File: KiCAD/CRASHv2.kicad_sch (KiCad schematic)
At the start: 2 parts, among them U1 ATmega32A-A, U2 LM317_SOT-223

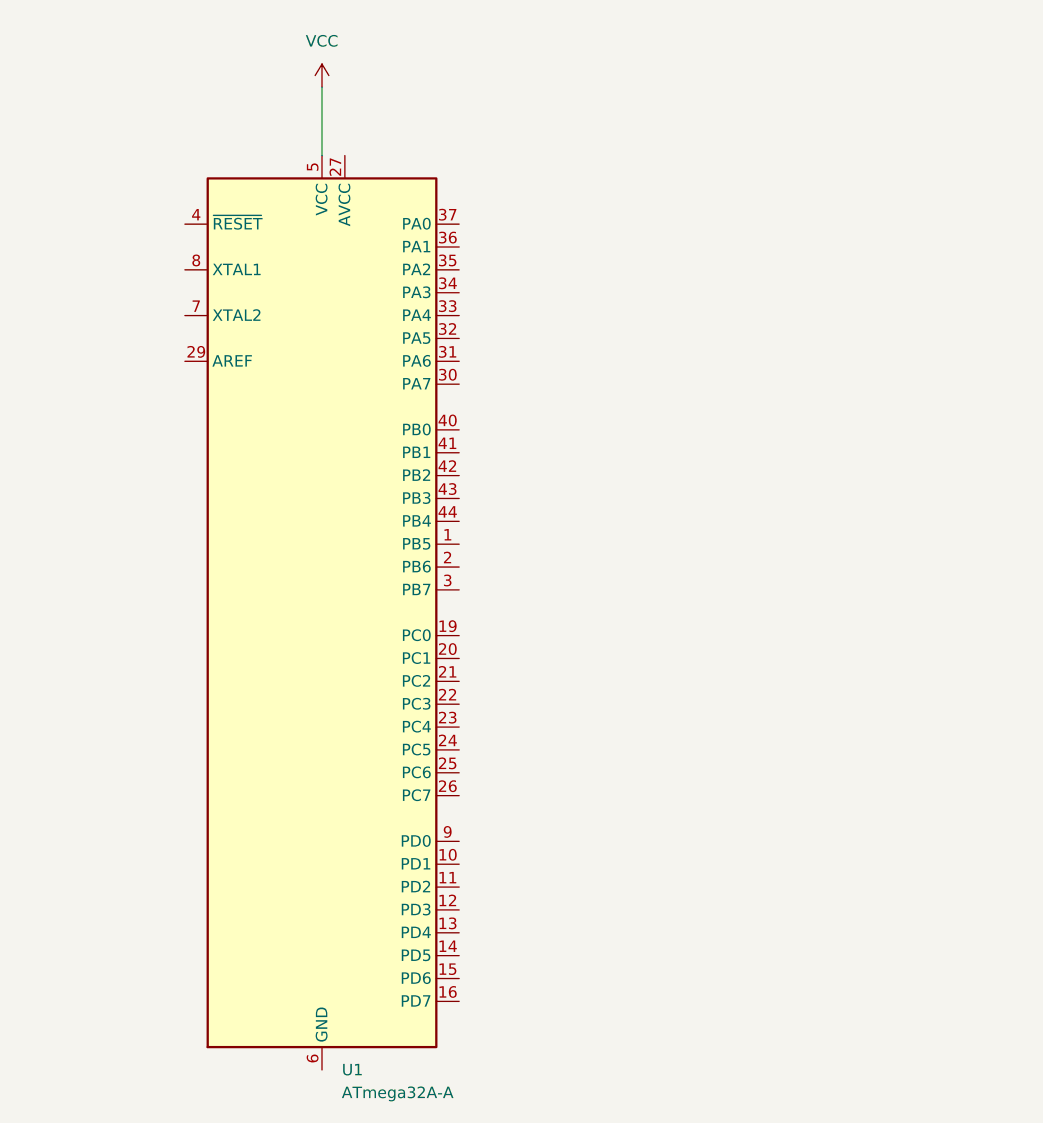
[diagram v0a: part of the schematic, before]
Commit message: Atmega ports for USB, nrf24 & gimble inputs
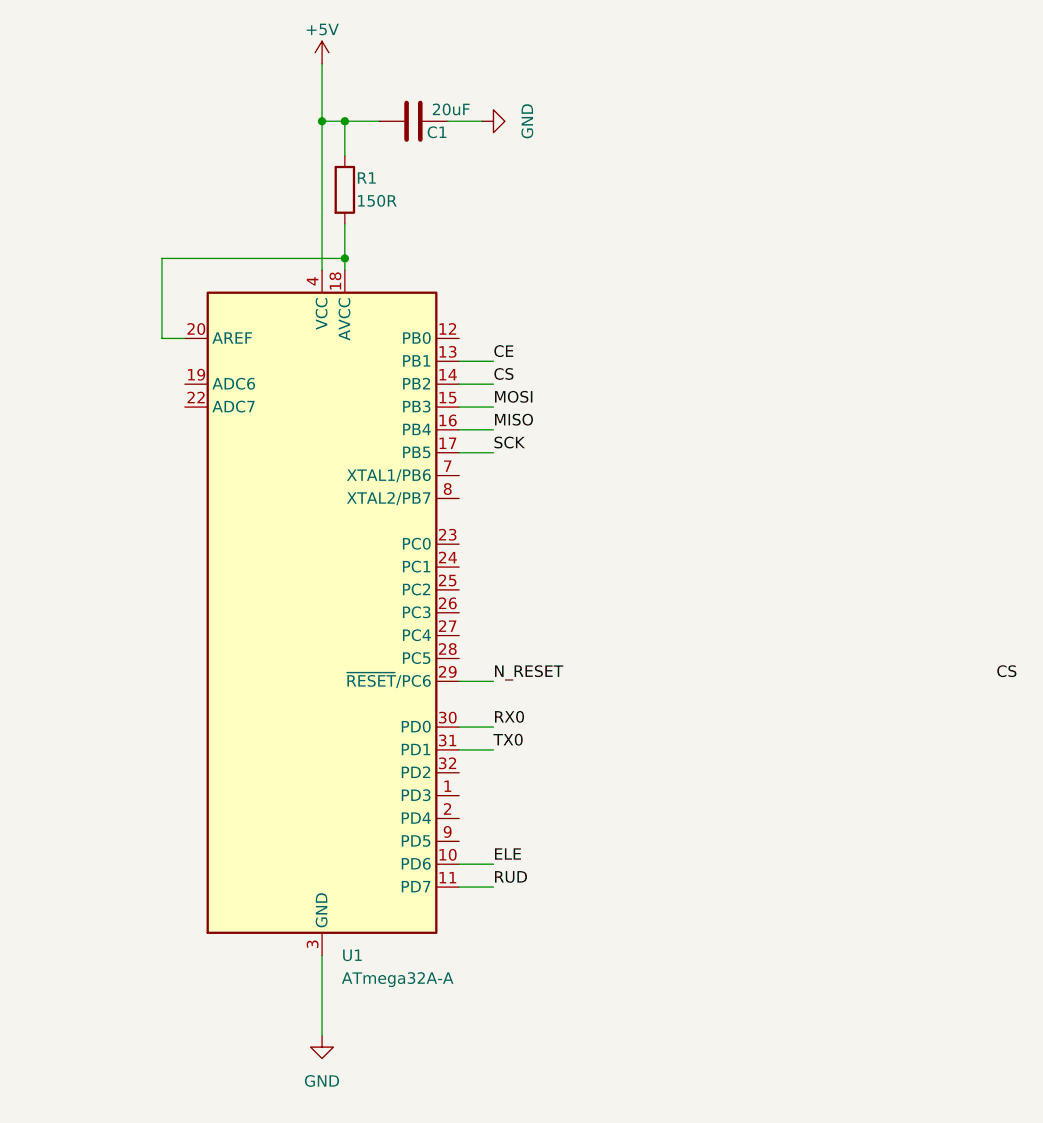
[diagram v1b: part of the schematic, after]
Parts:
- added C1: 20uF, symbol Device:C
- added R1: 150R, symbol Device:R
- U1: footprint Package_QFP:TQFP-44_10x10mm_P0.8mm -> Package_QFP:TQFP-32_7x7mm_P0.8mm; symbol MCU_Microchip_ATmega:ATmega32A-A -> MCU_Microchip_ATmega:ATmega328P-A
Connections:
- net ELE: now reaches U1.10 (PD6)
- net RUD: now reaches U1.11 (PD7)
- net CE: now reaches U1.13 (PB1)
- net CS: now reaches U1.14 (PB2)
- net MOSI: now reaches U1.15 (PB3)
- net MISO: now reaches U1.16 (PB4)
- net at U1.20 (AREF): now also U1.18 (AVCC), R1.2
- net GND: now reaches U1.21 (GND)
- net GND: now also U1.3 (GND), U1.5 (GND), C1.2
- net N_RESET: now reaches U1.29 (~{RESET}/PC6)
- net RX0: now reaches U1.30 (PD0)
- net TX0: now reaches U1.31 (PD1)
- net +5V: now reaches U1.4 (VCC)
- net +5V: now also U1.6 (VCC), C1.1, R1.1
- removed net VCC: U1.17 (VCC), U1.38 (VCC), U1.5 (VCC)
- new net SCK: U1.17 (PB5)
- now unconnected: U1.28 (GND)
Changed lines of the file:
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@@
 (kicad_sch (version 20230121) (generator eeschema)
   (paper "A4")
-  (wire (pts (xy 243.84 20.32) (xy 243.84 27.94))
-    (stroke (width 0) (type default))
+  (junction (at 246.38 24.13) (diameter 0) (color 0 0 0 0)
+  )
+  (junction (at 246.38 39.37) (diameter 0) (color 0 0 0 0)
+  )
+  (junction (at 243.84 24.13) (diameter 0) (color 0 0 0 0)
+  )
+  (wire (pts (xy 259.08 106.68) (xy 262.89 106.68))
+    (stroke (width 0) (type default))
+  )
+  (wire (pts (xy 259.08 53.34) (xy 262.89 53.34))
+    (stroke (width 0) (type default))
+  )
+  (wire (pts (xy 243.84 116.84) (xy 243.84 125.73))
+    (stroke (width 0) (type default))
+  )
+  (wire (pts (xy 259.08 86.36) (xy 262.89 86.36))
+    (stroke (width 0) (type default))
+  )
+  (wire (pts (xy 246.38 39.37) (xy 246.38 40.64))
+    (stroke (width 0) (type default))
+  )
+  (wire (pts (xy 246.38 24.13) (xy 250.19 24.13))
+    (stroke (width 0) (type default))
+  )
+  (wire (pts (xy 259.08 109.22) (xy 262.89 109.22))
+    (stroke (width 0) (type default))
+  )
+  (wire (pts (xy 228.6 48.26) (xy 226.06 48.26))
+    (stroke (width 0) (type default))
+  )
+  (wire (pts (xy 243.84 24.13) (xy 246.38 24.13))
+    (stroke (width 0) (type default))
+  )
+  (wire (pts (xy 243.84 24.13) (xy 243.84 40.64))
+    (stroke (width 0) (type default))
+  )
+  (wire (pts (xy 246.38 35.56) (xy 246.38 39.37))
+    (stroke (width 0) (type default))
+  )
+  (wire (pts (xy 259.08 50.8) (xy 262.89 50.8))
+    (stroke (width 0) (type default))
+  )
+  (wire (pts (xy 259.08 58.42) (xy 262.89 58.42))
+    (stroke (width 0) (type default))
+  )
+  (wire (pts (xy 259.08 55.88) (xy 262.89 55.88))
+    (stroke (width 0) (type default))
+  )
+  (wire (pts (xy 246.38 24.13) (xy 246.38 27.94))
+    (stroke (width 0) (type default))
+  )
+  (wire (pts (xy 243.84 17.78) (xy 243.84 24.13))
+    (stroke (width 0) (type default))
+  )
+  (wire (pts (xy 259.08 91.44) (xy 262.89 91.44))
+    (stroke (width 0) (type default))
+  )
+  (wire (pts (xy 226.06 48.26) (xy 226.06 39.37))
+    (stroke (width 0) (type default))
+  )
+  (wire (pts (xy 257.81 24.13) (xy 261.62 24.13))
+    (stroke (width 0) (type default))
+  )
+  (wire (pts (xy 259.08 60.96) (xy 262.89 60.96))
+    (stroke (width 0) (type default))
+  )
+  (wire (pts (xy 226.06 39.37) (xy 246.38 39.37))
+    (stroke (width 0) (type default))
+  )
+  (wire (pts (xy 259.08 93.98) (xy 262.89 93.98))
+    (stroke (width 0) (type default))
+  )
+  (label "RUD" (at 262.89 109.22 0) (fields_autoplaced)
+    (effects (font (size 1.27 1.27)) (justify left bottom))
+  )
+  (label "N_RESET" (at 262.89 86.36 0) (fields_autoplaced)
+    (effects (font (size 1.27 1.27)) (justify left bottom))
+  )
+  (label "TX0" (at 262.89 93.98 0) (fields_autoplaced)
+    (effects (font (size 1.27 1.27)) (justify left bottom))
+  )
+  (label "CE" (at 262.89 50.8 0) (fields_autoplaced)
+    (effects (font (size 1.27 1.27)) (justify left bottom))
+  )
+  (label "ELE" (at 262.89 106.68 0) (fields_autoplaced)
+    (effects (font (size 1.27 1.27)) (justify left bottom))
+  )
+  (label "CS" (at 262.89 53.34 0) (fields_autoplaced)
+    (effects (font (size 1.27 1.27)) (justify left bottom))
+  )
+  (label "MOSI" (at 262.89 55.88 0) (fields_autoplaced)
+    (effects (font (size 1.27 1.27)) (justify left bottom))
+  )
+  (label "MISO" (at 262.89 58.42 0) (fields_autoplaced)
+    (effects (font (size 1.27 1.27)) (justify left bottom))
+  )
+  (label "CS" (at 318.77 86.36 0) (fields_autoplaced)
+    (effects (font (size 1.27 1.27)) (justify left bottom))
+  )
+  (label "RX0" (at 262.89 91.44 0) (fields_autoplaced)
+    (effects (font (size 1.27 1.27)) (justify left bottom))
+  )
+  (label "SCK" (at 262.89 60.96 0) (fields_autoplaced)
+    (effects (font (size 1.27 1.27)) (justify left bottom))
+  )
+  (symbol (lib_id "Device:C") (at 254 24.13 90) (unit 1)
+    (in_bom yes) (on_board yes) (dnp no)
+    (property "Reference" "C1" (at 257.81 25.4 90)
+      (effects (font (size 1.27 1.27)) (justify left))
+    )
+    (property "Value" "20uF" (at 260.35 22.86 90)
+      (effects (font (size 1.27 1.27)) (justify left))
+    )
+    (property "Footprint" "" (at 257.81 23.1648 0)
+      (effects (font (size 1.27 1.27)) hide)
+    )
+    (property "Datasheet" "~" (at 254 24.13 0)
+      (effects (font (size 1.27 1.27)) hide)
+    )
+    (pin "1")
+    (pin "2")
+    (instances
+      (project "CRASHv2"
+        (path "/2cee430a-795a-4210-ade1-e98f5893d6a0"
+          (reference "C1") (unit 1)
+        )
+      )
+    )
+  )
+  (symbol (lib_id "Device:R") (at 246.38 31.75 0) (unit 1)
+    (in_bom yes) (on_board yes) (dnp no)
+    (property "Reference" "R1" (at 247.65 30.48 0)
+      (effects (font (size 1.27 1.27)) (justify left))
+    )
+    (property "Value" "150R" (at 247.65 33.02 0)
+      (effects (font (size 1.27 1.27)) (justify left))
+    )
+    (property "Footprint" "" (at 244.602 31.75 90)
+      (effects (font (size 1.27 1.27)) hide)
+    )
+    (property "Datasheet" "~" (at 246.38 31.75 0)
+      (effects (font (size 1.27 1.27)) hide)
+    )
+    (pin "1")
+    (pin "2")
+    (instances
+      (project "CRASHv2"
+        (path "/2cee430a-795a-4210-ade1-e98f5893d6a0"
+          (reference "R1") (unit 1)
+        )
+      )
+    )
   )
   (symbol (lib_id "Regulator_Linear:LM317_SOT-223") (at 62.23 44.45 0) (unit 1)
@@
     )
   )
-  (symbol (lib_id "MCU_Microchip_ATmega:ATmega32A-A") (at 243.84 78.74 0) (unit 1)
+  (symbol (lib_id "MCU_Microchip_ATmega:ATmega328P-A") (at 243.84 78.74 0) (unit 1)
     (in_bom yes) (on_board yes) (dnp no) (fields_autoplaced)
-    (property "Reference" "U1" (at 246.0341 129.54 0)
-      (effects (font (size 1.27 1.27)) (justify left))
-    )
-    (property "Value" "ATmega32A-A" (at 246.0341 132.08 0)
-      (effects (font (size 1.27 1.27)) (justify left))
-    )
-    (property "Footprint" "Package_QFP:TQFP-44_10x10mm_P0.8mm" (at 243.84 78.74 0)
+    (property "Reference" "U1" (at 246.0341 116.84 0)
+      (effects (font (size 1.27 1.27)) (justify left))
+    )
+    (property "Value" "ATmega32A-A" (at 246.0341 119.38 0)
+      (effects (font (size 1.27 1.27)) (justify left))
+    )
+    (property "Footprint" "Package_QFP:TQFP-32_7x7mm_P0.8mm" (at 243.84 78.74 0)
       (effects (font (size 1.27 1.27) italic) hide)
     )
-    (property "Datasheet" "http://ww1.microchip.com/downloads/en/DeviceDoc/atmel-8155-8-bit-microcontroller-avr-atmega32a_datasheet.pdf" (at 243.84 78.74 0)
+    (property "Datasheet" "http://ww1.microchip.com/downloads/en/DeviceDoc/ATmega328_P%20AVR%20MCU%20with%20picoPower%20Technology%20Data%20Sheet%2040001984A.pdf" (at 243.84 78.74 0)
       (effects (font (size 1.27 1.27)) hide)
     )
@@
     (pin "31")
     (pin "32")
-    (pin "33")
-    (pin "34")
-    (pin "35")
-    (pin "36")
-    (pin "37")
-    (pin "38")
-    (pin "39")
     (pin "4")
-    (pin "40")
-    (pin "41")
-    (pin "42")
-    (pin "43")
-    (pin "44")
     (pin "5")
     (pin "6")
@@
     )
   )
-  (symbol (lib_id "power:VCC") (at 243.84 20.32 0) (unit 1)
+  (symbol (lib_id "power:GND") (at 243.84 125.73 0) (unit 1)
     (in_bom yes) (on_board yes) (dnp no) (fields_autoplaced)
-    (property "Reference" "#PWR01" (at 243.84 24.13 0)
-      (effects (font (size 1.27 1.27)) hide)
-    )
-    (property "Value" "VCC" (at 243.84 15.24 0)
-      (effects (font (size 1.27 1.27)))
-    )
-    (property "Footprint" "" (at 243.84 20.32 0)
-      (effects (font (size 1.27 1.27)) hide)
-    )
-    (property "Datasheet" "" (at 243.84 20.32 0)
+    (property "Reference" "#PWR02" (at 243.84 132.08 0)
+      (effects (font (size 1.27 1.27)) hide)
+    )
+    (property "Value" "GND" (at 243.84 130.81 0)
+      (effects (font (size 1.27 1.27)))
+    )
+    (property "Footprint" "" (at 243.84 125.73 0)
+      (effects (font (size 1.27 1.27)) hide)
+    )
+    (property "Datasheet" "" (at 243.84 125.73 0)
+      (effects (font (size 1.27 1.27)) hide)
+    )
+    (pin "1")
+    (instances
+      (project "CRASHv2"
+        (path "/2cee430a-795a-4210-ade1-e98f5893d6a0"
+          (reference "#PWR02") (unit 1)
+        )
+      )
+    )
+  )
+  (symbol (lib_id "power:+5V") (at 243.84 17.78 0) (unit 1)
+    (in_bom yes) (on_board yes) (dnp no)
+    (property "Reference" "#PWR01" (at 243.84 21.59 0)
+      (effects (font (size 1.27 1.27)) hide)
+    )
+    (property "Value" "+5V" (at 243.84 13.97 0)
+      (effects (font (size 1.27 1.27)))
+    )
+    (property "Footprint" "" (at 243.84 17.78 0)
+      (effects (font (size 1.27 1.27)) hide)
+    )
+    (property "Datasheet" "" (at 243.84 17.78 0)
       (effects (font (size 1.27 1.27)) hide)
     )
@@
         )
       )
+    )
+  )
+  (symbol (lib_id "power:GND") (at 261.62 24.13 90) (unit 1)
+    (in_bom yes) (on_board yes) (dnp no) (fields_autoplaced)
+    (property "Reference" "#PWR03" (at 267.97 24.13 0)
+      (effects (font (size 1.27 1.27)) hide)
+    )
+    (property "Value" "GND" (at 266.7 24.13 0)
+      (effects (font (size 1.27 1.27)))
+    )
+    (property "Footprint" "" (at 261.62 24.13 0)
+      (effects (font (size 1.27 1.27)) hide)
+    )
+    (property "Datasheet" "" (at 261.62 24.13 0)
+      (effects (font (size 1.27 1.27)) hide)
+    )
+    (pin "1")
+    (instances
+      (project "CRASHv2"
+        (path "/2cee430a-795a-4210-ade1-e98f5893d6a0"
+          (reference "#PWR03") (unit 1)
+        )
+      )
